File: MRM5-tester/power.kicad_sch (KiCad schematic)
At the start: 18 parts, among them IC1 ADPL16000AATA+T, IC2 REF35160QDBVR

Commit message: tester updated 회로도 제작중
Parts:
- removed C10: 0.1u, PCM_Capacitor_SMD_AKL:C_0402_1005Metric, symbol PCM_Capacitor_AKL:C_0402
- removed C11, C13, C9: 1u, PCM_Capacitor_SMD_AKL:C_0402_1005Metric, symbol PCM_Capacitor_AKL:C_0402
- removed C12: 10u, PCM_Capacitor_SMD_AKL:C_0805_2012Metric_Pad1.15x1.40mm, symbol PCM_Capacitor_AKL:C_0402
- removed C14: 22u, PCM_Capacitor_SMD_AKL:C_0805_2012Metric_Pad1.15x1.40mm, symbol PCM_Capacitor_AKL:C_0402
- removed IC1: ADPL16000AATA+T, Mouser:ADPL16000AATAT, symbol Mouser:ADPL16000AATA+T
- removed IC2: REF35160QDBVR, Mouser:SOT95P280X145-6N, symbol Mouser:REF35160QDBVR
- removed L1: CBC3225T470KR, Mouser:INDC3225X270N, symbol Mouser:CBC3225T470KR
- removed R8: 3.65k, PCM_Resistor_SMD_AKL:R_0402_1005Metric, symbol PCM_Resistor_AKL:R_0402
- added PS2: LD39200DPUR, SON80P400X400X100-9N-D, symbol Mouser:LD39200DPUR
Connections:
- no-connect marks 1 -> 0

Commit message: tester updated
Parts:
- added R11: 47.5k, PCM_Resistor_SMD_AKL:R_0402_1005Metric, symbol PCM_Resistor_AKL:R_0402
- added R8: 22.1k, PCM_Resistor_SMD_AKL:R_0402_1005Metric, symbol PCM_Resistor_AKL:R_0402
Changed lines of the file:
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@@
+	)
+	(symbol
+		(lib_id "PCM_Resistor_AKL:R_0402")
+		(at 193.04 135.89 180)
+		(unit 1)
+		(exclude_from_sim no)
+		(in_bom yes)
+		(on_board yes)
+		(dnp no)
+		(fields_autoplaced yes)
+		(property "Reference" "R11"
+			(at 195.58 134.6199 0)
+			(effects
+				(font
+					(size 1.27 1.27)
+				)
+				(justify right)
+			)
+		)
+		(property "Value" "47.5k"
+			(at 195.58 137.1599 0)
+			(effects
+				(font
+					(size 1.27 1.27)
+				)
+				(justify right)
+			)
+		)
+		(property "Footprint" "PCM_Resistor_SMD_AKL:R_0402_1005Metric"
+			(at 193.04 124.46 0)
+			(effects
+				(font
+					(size 1.27 1.27)
+				)
+				(hide yes)
+			)
+		)
+		(property "Datasheet" "~"
+			(at 193.04 135.89 0)
+			(effects
+				(font
+					(size 1.27 1.27)
+				)
+				(hide yes)
+			)
+		)
+		(property "Description" "SMD 0402 Chip Resistor, European Symbol, Alternate KiCad Library"
+			(at 193.04 135.89 0)
+			(effects
+				(font
+					(size 1.27 1.27)
+				)
+				(hide yes)
+			)
+		)
+		(pin "2"
+		)
+		(pin "1"
+		)
+		(instances
+			(project "MRM5-tester"
+				(path "/6e775c75-0b09-4e5f-9bff-c5585ac94ad7/c69ac902-00f4-4f29-a9f3-8d3beb585abf"
+					(reference "R11")
+					(unit 1)
+				)
+			)
+		)
 	)
 	(symbol
@@
 					(unit 1)
 				)
+			)
+		)
+	)
+	(symbol
+		(lib_id "PCM_Resistor_AKL:R_0402")
+		(at 193.04 113.03 180)
+		(unit 1)
+		(exclude_from_sim no)
+		(in_bom yes)
+		(on_board yes)
+		(dnp no)
+		(fields_autoplaced yes)
+		(property "Reference" "R8"
+			(at 195.58 111.7599 0)
+			(effects
+				(font
+					(size 1.27 1.27)
+				)
+				(justify right)
+			)
+		)
+		(property "Value" "22.1k"
+			(at 195.58 114.2999 0)
+			(effects
+				(font
+					(size 1.27 1.27)
+				)
+				(justify right)
+			)
+		)
+		(property "Footprint" "PCM_Resistor_SMD_AKL:R_0402_1005Metric"
+			(at 193.04 101.6 0)
+			(effects
+				(font
+					(size 1.27 1.27)
+				)
+				(hide yes)
+			)
+		)
+		(property "Datasheet" "~"
+			(at 193.04 113.03 0)
+			(effects
+				(font
+					(size 1.27 1.27)
+				)
+				(hide yes)
+			)
+		)
+		(property "Description" "SMD 0402 Chip Resistor, European Symbol, Alternate KiCad Library"
+			(at 193.04 113.03 0)
+			(effects
+				(font
+					(size 1.27 1.27)
+				)
+				(hide yes)
+			)
+		)
+		(pin "2"
+		)
+		(pin "1"
+		)
+		(instances
+			(project "MRM5-tester"
+				(path "/6e775c75-0b09-4e5f-9bff-c5585ac94ad7/c69ac902-00f4-4f29-a9f3-8d3beb585abf"
+					(reference "R8")
+					(unit 1)
+				)

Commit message: tester PCB 작성중
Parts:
- removed C15: B32922X2104K000, B32922X_(18_X_5), symbol Mouser:B32922X2104K000
- removed FL1: SSHB10HS-R11100, SSHB10HSR11100, symbol Mouser:SSHB10HS-R11100
- removed P1, P2: ~, Mouser:PAD_hole, symbol Mouser:PAD_hole2.6
- removed PS2: LD39200DPUR, SON80P400X400X100-9N-D, symbol Mouser:LD39200DPUR
- removed R11: 47.5k, PCM_Resistor_SMD_AKL:R_0402_1005Metric, symbol PCM_Resistor_AKL:R_0402
- removed R8: 22.1k, PCM_Resistor_SMD_AKL:R_0402_1005Metric, symbol PCM_Resistor_AKL:R_0402
- added C15, C17: 10uF_16V, Capacitor_THT:CP_Radial_D5.0mm_P2.00mm, symbol PCM_SL_Capacitors:10uF_16V
- added C16: B32922X2104K000, Mouser:B32922X__18_X_5_, symbol ktw07182:B32922X2104K000
- added FL1: SSHB10HS-R11100, Mouser:SSHB10HSR11100, symbol ktw07182:SSHB10HS-R11100
- added IC3: LM1085IS-3.3/NOPB, Mouser:KTT0003B, symbol ktw07182:LM1085ISX-ADJ_NOPB
- added IC4: OPA567AIRHGT, Mouser:QFN100P500X500X100-13N-D, symbol Mouser:OPA567AIRHGT
- added R23, R24, R26: 7.68k, PCM_Resistor_SMD_AKL:R_0402_1005Metric, symbol PCM_Resistor_AKL:R_0402
- PS1: footprint HLK15M05C -> Mouser:HLK15M05C
- RT1: footprint NTC10D11 -> Mouser:NTC10D11
- RV1: footprint MOV10D391K -> Mouser:MOV10D391K
- renumbered C16 to C18
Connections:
- net 5V: now also C15.1, IC3.3 (INPUT)
- net GND: now also C15.2, C17.2, IC3.1 (ADJ/GND), IC4.4 (V-_1), IC4.5 (V-_2), R23.2, R26.2
- net Vn_h: now reaches RV1.1
- net Vn_h: now also C16.1, FL1.2
- net Vp_sh: now reaches RT1.2
- net Vp_sh: now also C16.2, FL1.1
- net at PS1.2 (AC_2): now also FL1.3
- net at PS1.1 (AC_1): now also FL1.4
- net Vp_h: now reaches RT1.1, RV1.2
- new net: IC4.6 (ISET), R26.1
- new net: IC4.9 (+IN), R23.1, R24.2
- new net 1V6: IC4.13 (EP), IC4.2 (V_O_1), IC4.3 (V_O_2), IC4.8 (-IN)
- new net 1V6_IFlag: IC4.7 (IFLAG)
- new net 1V6_TFlag: IC4.10 (TFLAG), IC4.11 (ENABLE)
- new net 3V3: C17.1, IC3.2 (OUTPUT), IC3.4 (TAB_(VOUT)), IC4.1 (V+_1), IC4.12 (V+_2), R24.1
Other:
- moved on the sheet: C18, PS1, RT1, RV1

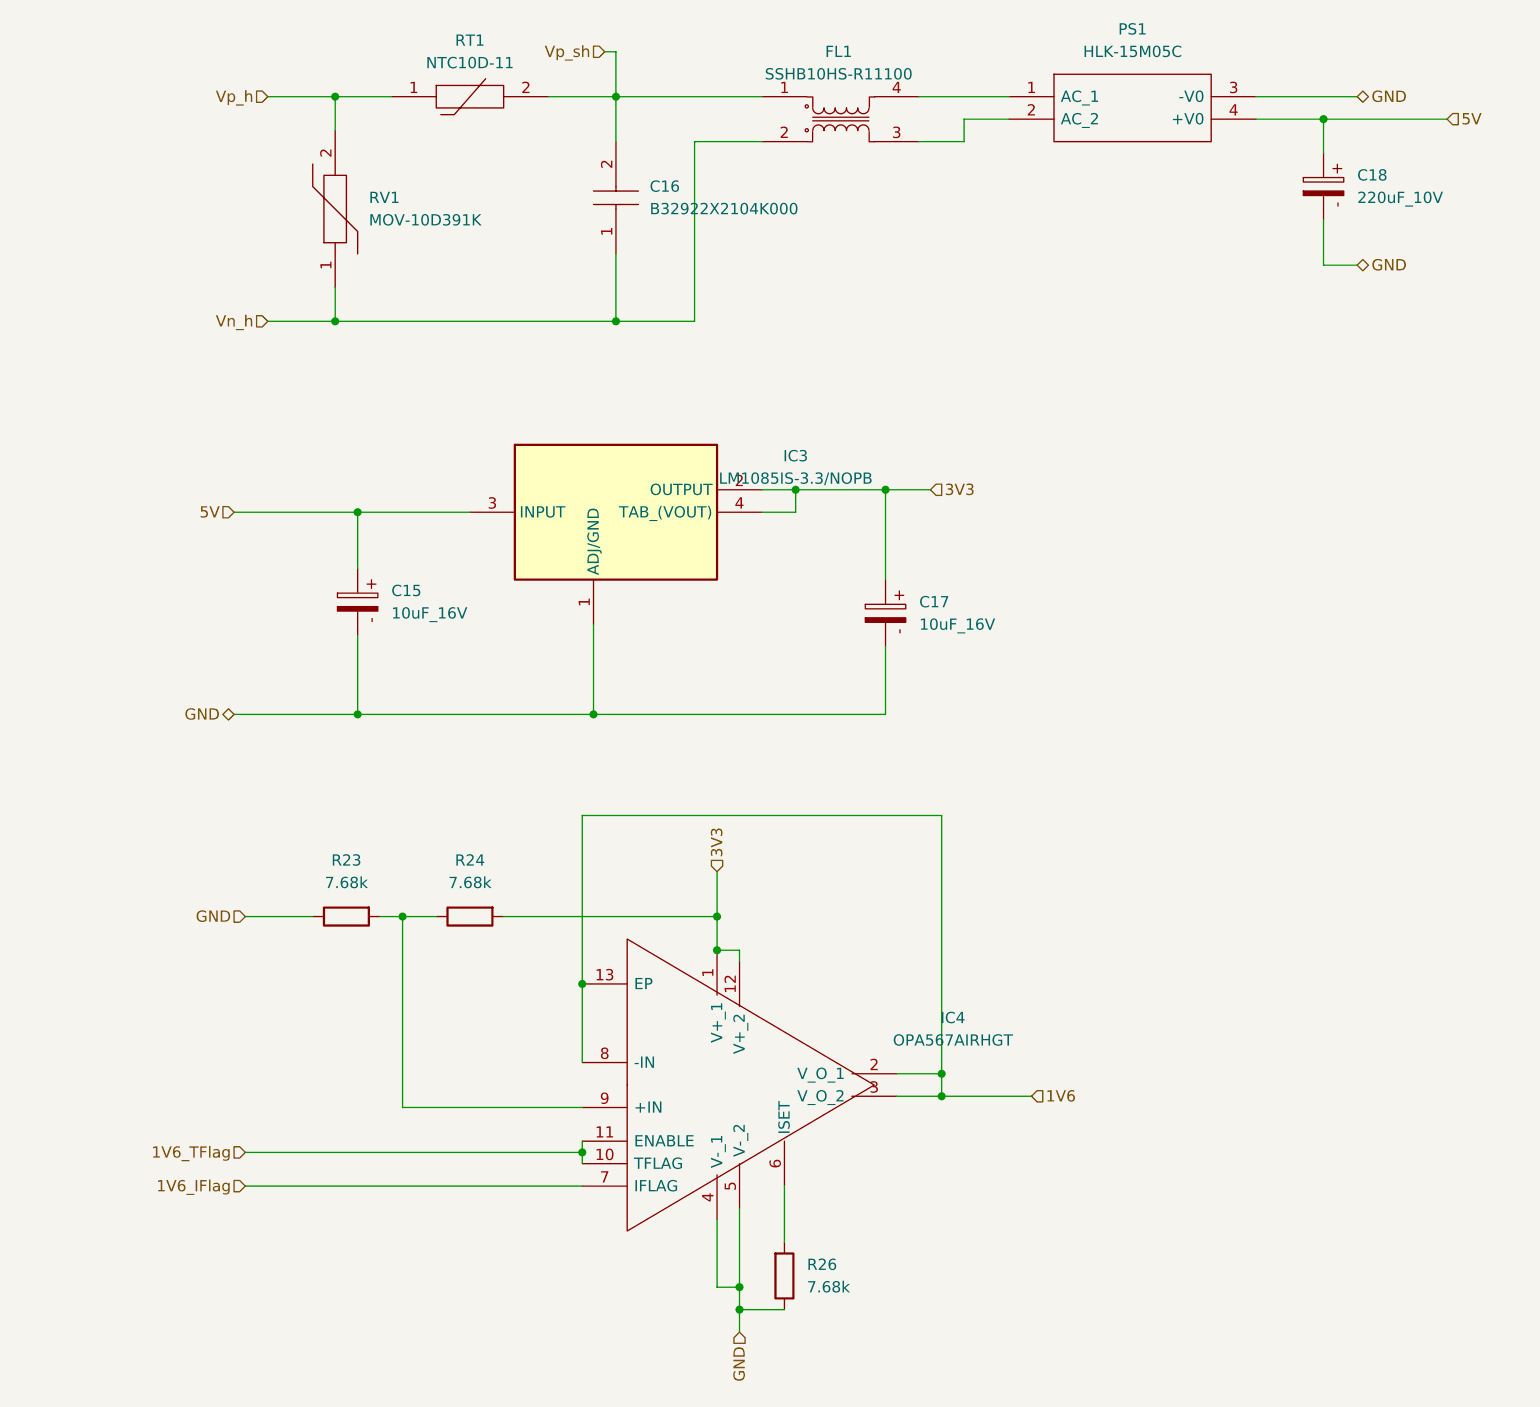
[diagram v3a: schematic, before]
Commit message: tester pcb 디자인 완료
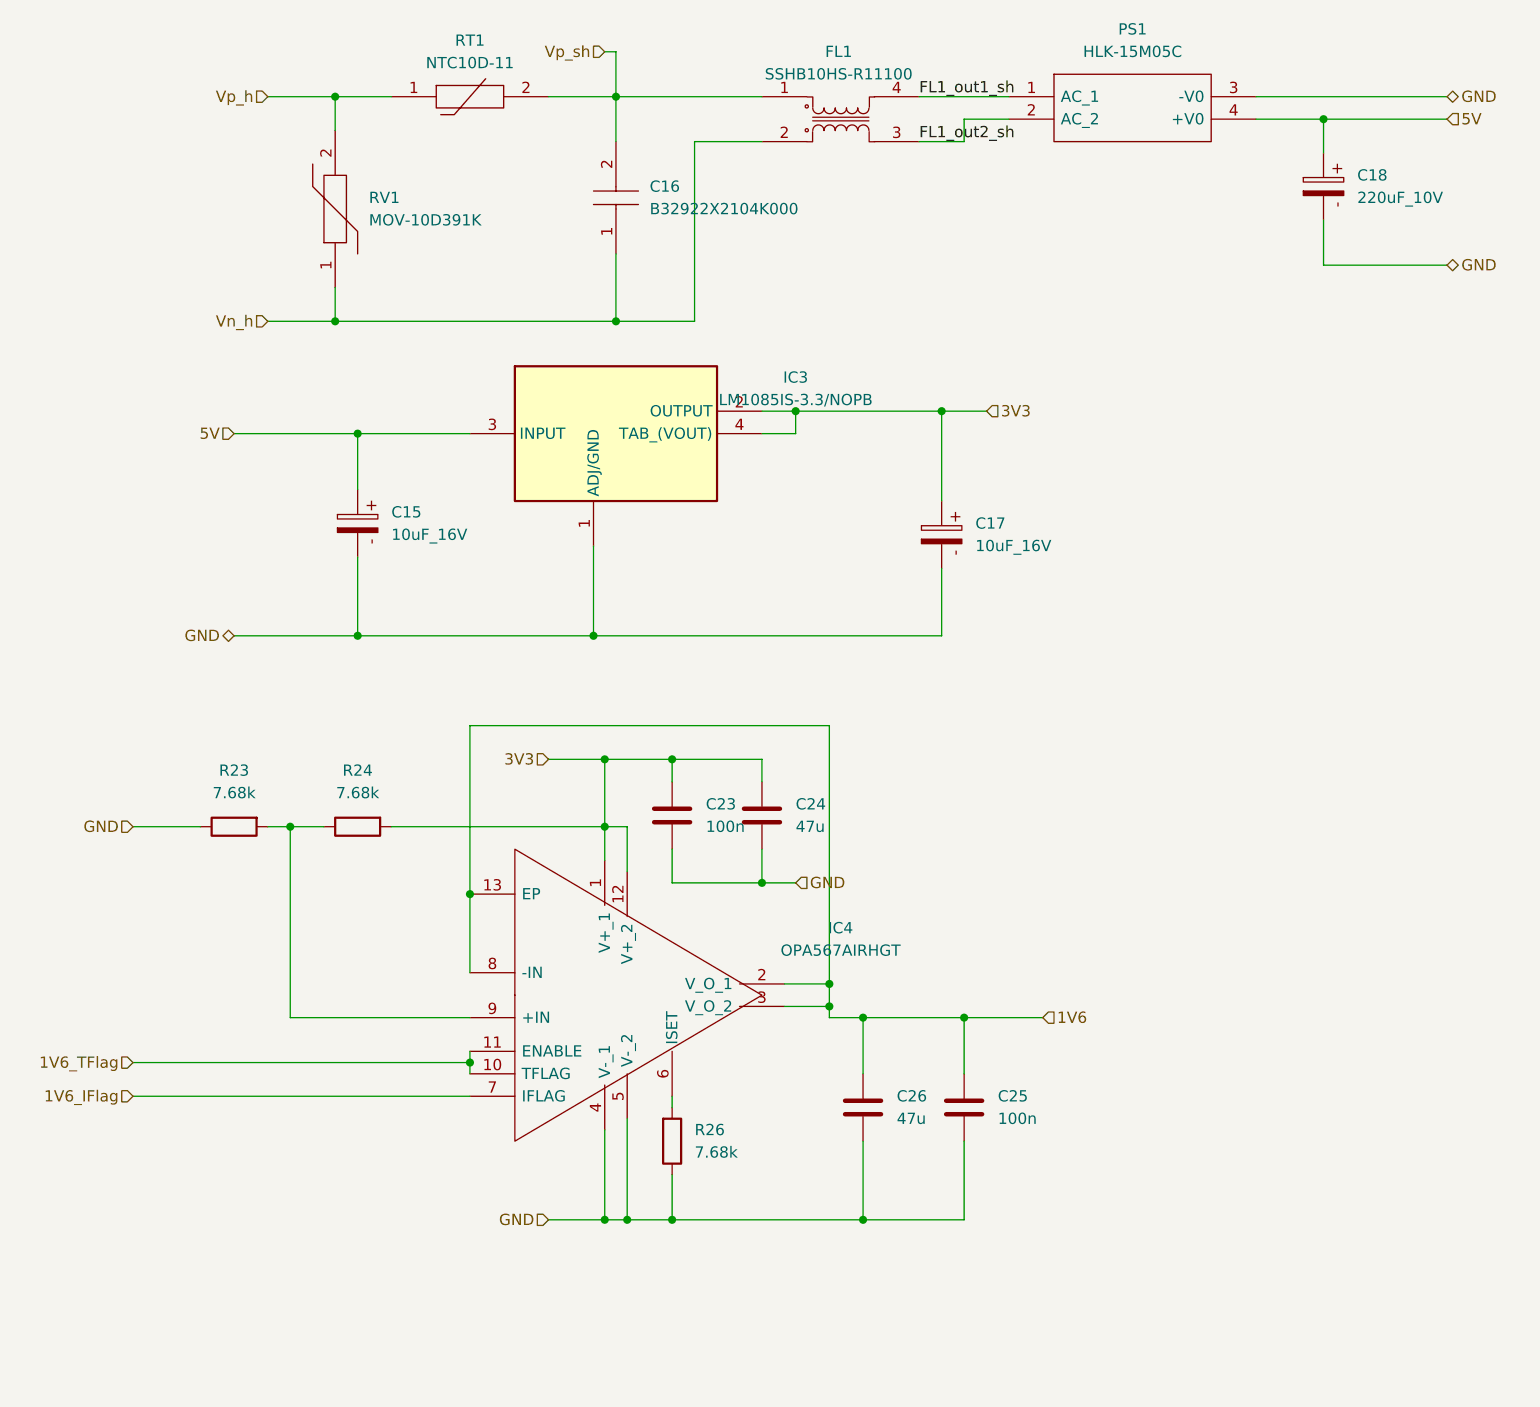
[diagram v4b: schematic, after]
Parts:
- added C23, C25: 100n, PCM_Capacitor_SMD_AKL:C_0402_1005Metric, symbol PCM_Capacitor_AKL:C_0402
- added C24, C26: 47u, PCM_Capacitor_SMD_AKL:C_0603_1608Metric, symbol PCM_Capacitor_AKL:C_0603
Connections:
- net 1V6: now also C25.2, C26.1
- net 3V3: now also C23.2, C24.1
- net GND: now also C23.1, C24.2, C25.1, C26.2
- net FL1_out2_sh: now reaches FL1.3, PS1.2 (AC_2)
- net FL1_out1_sh: now reaches FL1.4, PS1.1 (AC_1)
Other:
- moved on the sheet: C15, C17, IC3, IC4, R23, R24, R26

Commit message: tester PCB 검토
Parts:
- C15, C17: footprint Capacitor_THT:CP_Radial_D5.0mm_P2.00mm -> Capacitor_THT:C_Radial_D5.0mm_H11.0mm_P2.00mm
- C18: value 220uF_10V -> 220uF 16V 105℃; footprint Capacitor_THT:CP_Radial_D6.3mm_P2.50mm -> Capacitor_THT:C_Radial_D6.3mm_H11.0mm_P2.50mm
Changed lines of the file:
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@@
 			)
 		)
-		(property "Footprint" "Capacitor_THT:CP_Radial_D5.0mm_P2.00mm"
+		(property "Footprint" "Capacitor_THT:C_Radial_D5.0mm_H11.0mm_P2.00mm"
 			(at 157.48 85.852 0)
 			(effects
@@
 			)
 		)
-		(property "Footprint" "Capacitor_THT:CP_Radial_D5.0mm_P2.00mm"
+		(property "Footprint" "Capacitor_THT:C_Radial_D5.0mm_H11.0mm_P2.00mm"
 			(at 91.44 84.582 0)
 			(effects
@@
 			)
 		)
-		(property "Value" "220uF_10V"
+		(property "Value" "220uF 16V 105℃"
 			(at 208.28 46.9899 90)
 			(effects
@@
 			)
 		)
-		(property "Footprint" "Capacitor_THT:CP_Radial_D6.3mm_P2.50mm"
+		(property "Footprint" "Capacitor_THT:C_Radial_D6.3mm_H11.0mm_P2.50mm"
 			(at 200.66 46.482 0)
 			(effects

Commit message: MRM5-tester updated
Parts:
- removed C15, C17: 10uF_16V, Capacitor_THT:C_Radial_D5.0mm_H11.0mm_P2.00mm, symbol PCM_SL_Capacitors:10uF_16V
- removed IC3: LM1085IS-3.3/NOPB, Mouser:KTT0003B, symbol ktw07182:LM1085ISX-ADJ_NOPB
- added C19, C24: 10uF, 16V, PCM_Capacitor_SMD_AKL:C_0603_1608Metric, symbol PCM_Capacitor_AKL:C_0603
- added IC5: LD1085D2T33R, Mouser:LD1085D2T33R, symbol ktw07182:LD1085D2T33R
- FL1: value SSHB10HS-R11100 -> SS21V-R110100
- renumbered C16 to C20, C23 to C21, C24 to C22, C26 to C23, C18 to C26, IC4 to IC3, R23 to R25, R24 to R26, R26 to R27
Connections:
- net 3V3: now also C24.1, IC5.4 (OUTPUT)
- net 5V: now also C19.1, IC5.3 (INPUT)
- net GND: now also C19.2, C24.2, IC5.1 (GND)

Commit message: tester pcb updated
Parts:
- renumbered IC5 to IC3, IC3 to IC4
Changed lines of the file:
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@@
 	)
 	(image
-		(at 215.9 88.9)
+		(at 215.9 87.63)
 		(data "iVBORw0KGgoAAAANSUhEUgAAArIAAAFSCAYAAAAO1TyfAAAABHNCSVQICAgIfAhkiAAAABl0RVh0"
 			"U29mdHdhcmUAZ25vbWUtc2NyZWVuc2hvdO8Dvz4AAABEaVRYdENyZWF0aW9uIFRpbWUAAAAAADIw"
@@
 		(dnp no)
 		(fields_autoplaced yes)
-		(property "Reference" "IC5"
+		(property "Reference" "IC3"
 			(at 128.27 66.04 0)
 			(effects
@@
 			(project ""
 				(path "/6e775c75-0b09-4e5f-9bff-c5585ac94ad7/c69ac902-00f4-4f29-a9f3-8d3beb585abf"
-					(reference "IC5")
+					(reference "IC3")
 					(unit 1)
 				)
@@
 		(dnp no)
 		(fields_autoplaced yes)
-		(property "Reference" "IC3"
+		(property "Reference" "IC4"
 			(at 149.86 129.5714 0)
 			(effects
@@
 			(project "MRM5-tester"
 				(path "/6e775c75-0b09-4e5f-9bff-c5585ac94ad7/c69ac902-00f4-4f29-a9f3-8d3beb585abf"
-					(reference "IC3")
+					(reference "IC4")
 					(unit 1)
 				)
